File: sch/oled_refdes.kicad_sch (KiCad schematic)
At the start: 12 parts, among them J1 SH1106G

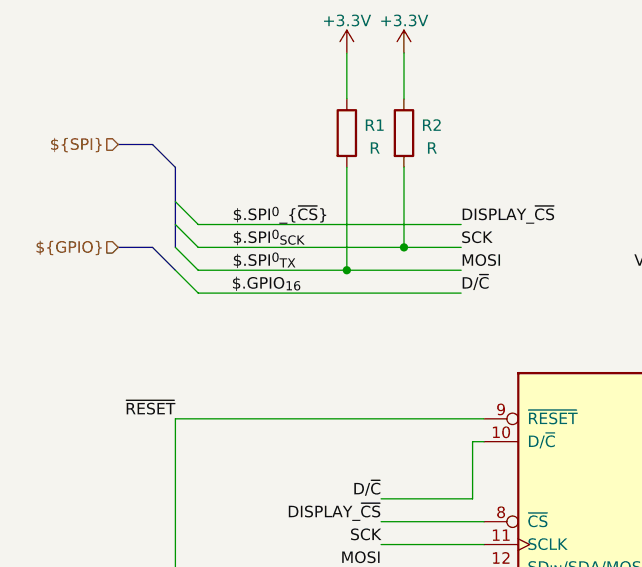
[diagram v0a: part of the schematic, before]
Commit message: Fixed SPI pin assignments to SPI0 only
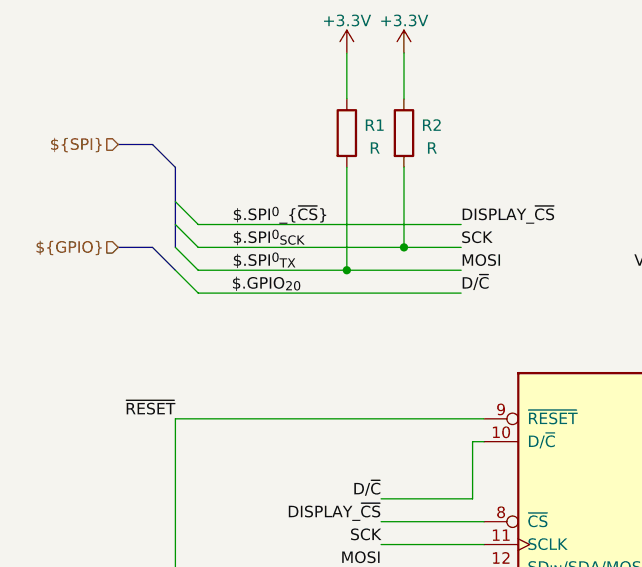
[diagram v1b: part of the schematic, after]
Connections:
- net $.GPIO_{16} renamed $.GPIO_{20}
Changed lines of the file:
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@@
     (effects (font (size 1.27 1.27)) (justify right bottom))
   )
-  (label "$.GPIO_{16}" (at 68.58 74.93 180)
+  (label "$.GPIO_{20}" (at 68.58 74.93 180)
     (effects (font (size 1.27 1.27)) (justify right bottom))
   )
